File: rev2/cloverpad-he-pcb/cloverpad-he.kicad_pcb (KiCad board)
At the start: 2 copper layers, 70 x 75 mm, 51 parts, among them J1 USB_C_Receptacle_USB2.0, SW1 SW_Push, SW2 SW_Push, U1 SRV05-4, U2 XC6206P332MR, U3 DRV5056AxxDBZxQ1, U4 DRV5056AxxDBZxQ1, U5 DRV5056AxxDBZxQ1, U8 RP2040, U9 W25Q16JVSSIQ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

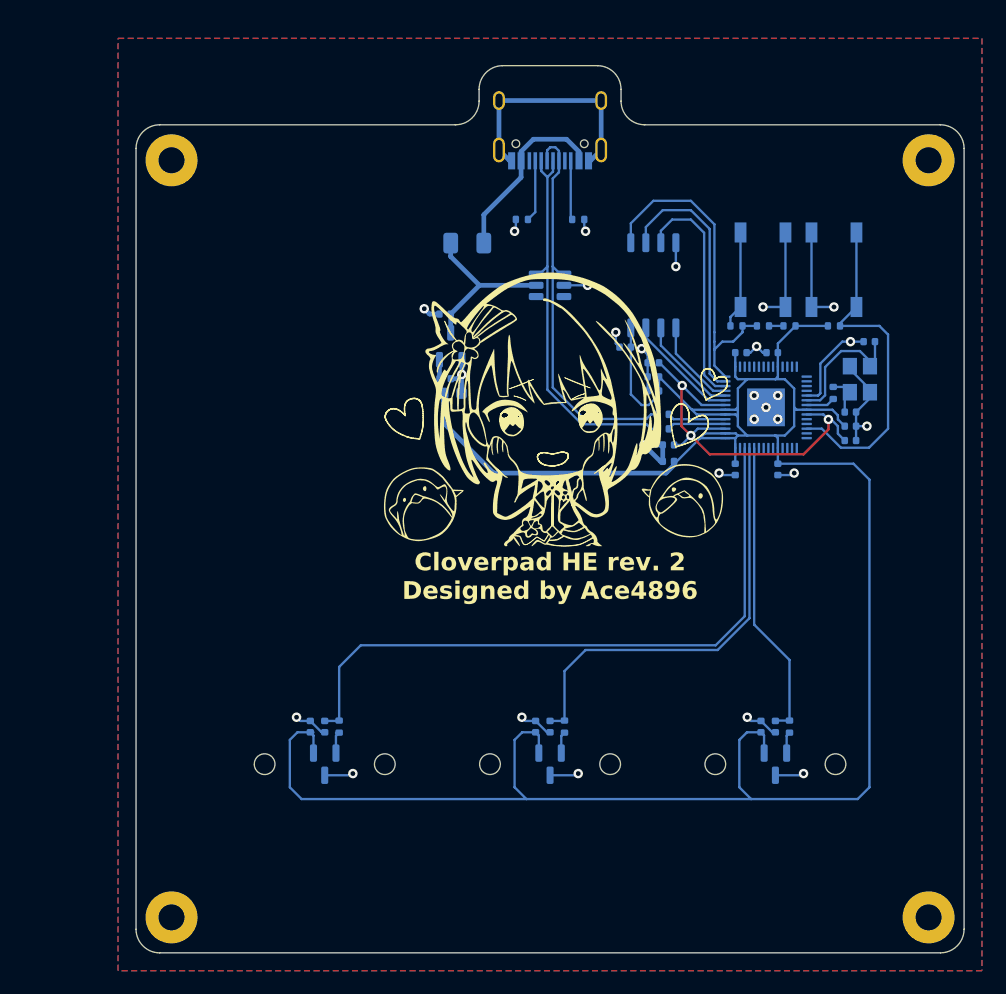
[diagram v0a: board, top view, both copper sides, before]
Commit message: feat(r2): initial attempt at shrinking case + pcb
Case: 75x65mm, PCB: 60x50mm (57.5mm height including USB-C cutout)

I'm able to get ~3mm wall thickness around the threaded inserts, which gives me a bit more confidence in the walls not cracking.
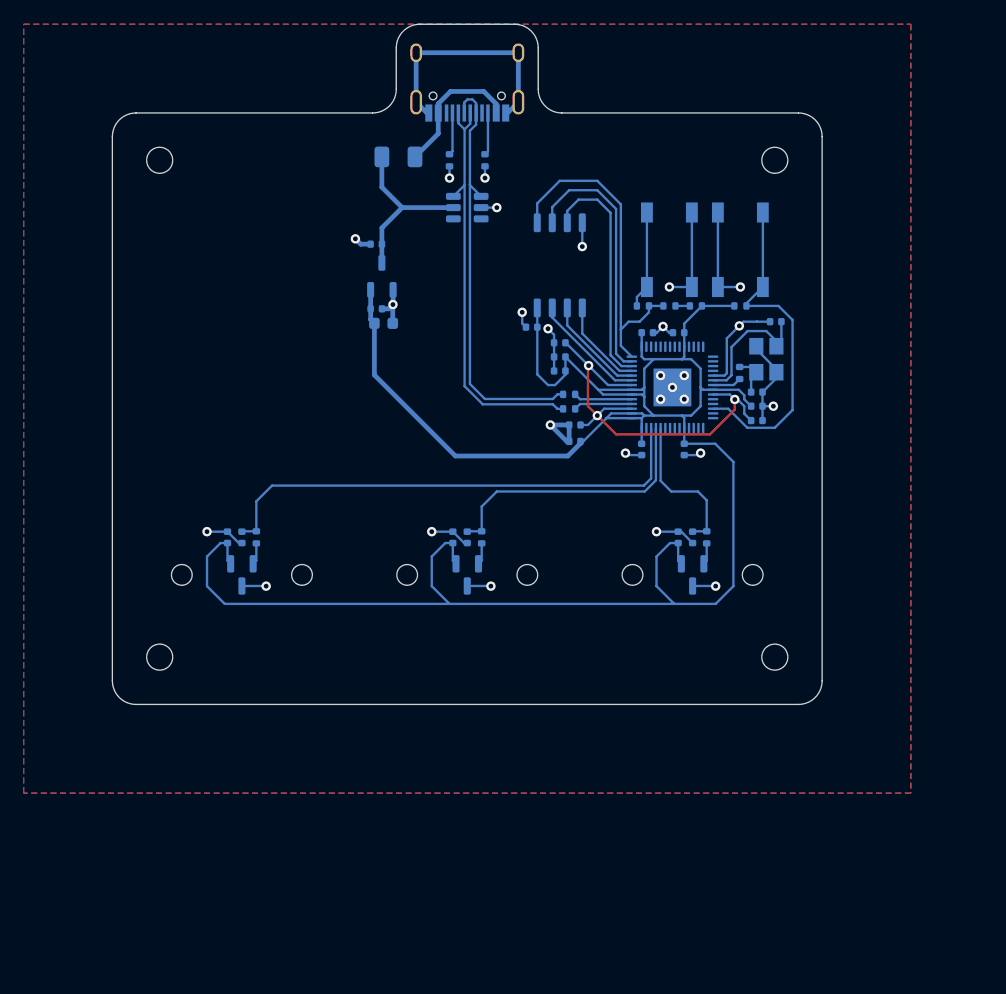
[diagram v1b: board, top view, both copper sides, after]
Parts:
- H1, H2, H3, H4: footprint MountingHole:MountingHole_2.2mm_M2_Pad -> MountingHole:MountingHole_2.2mm_M2
- moved H4 25.6 mm to (79.8, 70.8)
- moved H3 22.0 mm to (27.8, 70.8)
- moved C1 17.5 mm to (33.5, 60.7)
- moved C2 17.5 mm to (52.6, 60.7)
- moved C6 17.5 mm to (34.8, 60.7)
- moved C7 17.5 mm to (53.8, 60.7)
- moved C8 17.5 mm to (72.9, 60.7)
- moved R3 17.5 mm to (36.0, 60.7)
- moved R4 17.5 mm to (55.0, 60.7)
- moved C3 17.5 mm to (71.6, 60.7)
- moved R5 17.5 mm to (74.0, 60.7)
- moved U3 17.5 mm to (34.7, 63.9)
- moved U4 17.5 mm to (53.8, 63.9)
- moved U5 17.5 mm to (72.9, 63.9)
- moved H2 13.0 mm to (79.8, 28.8)
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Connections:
- net VBUS renamed Net-(F1-Pad2)
- J1 pad A8: (no net) -> unconnected-(J1-SBU1-PadA8)
- J1 pad B8: (no net) -> unconnected-(J1-SBU2-PadB8)
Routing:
- net +3V3: track 208.9 -> 184.2 mm
- net HS1: track 37.3 -> 23.4 mm
- net HS0: track 56.0 -> 42.2 mm
- net HS2: track 25.5 -> 12.9 mm
- net Net-(F1-Pad2): track 15.6 -> 11.8 mm
- net D+: track 33.6 -> 36.1 mm
- net D-: track 33.0 -> 35.4 mm
- net Net-(J1-CC1): track 5.21 -> 3.59 mm
- net Net-(J1-CC2): track 5.01 -> 3.59 mm
- net RESET: track 29.0 -> 28.5 mm
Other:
- board size 70 x 75 mm -> 60 x 57.5 mm
- board text removed: "Cloverpad HE rev. 2 Designed by Ace4896"
